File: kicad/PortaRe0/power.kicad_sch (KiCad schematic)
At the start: 18 parts, among them U1 BQ25895RTWR

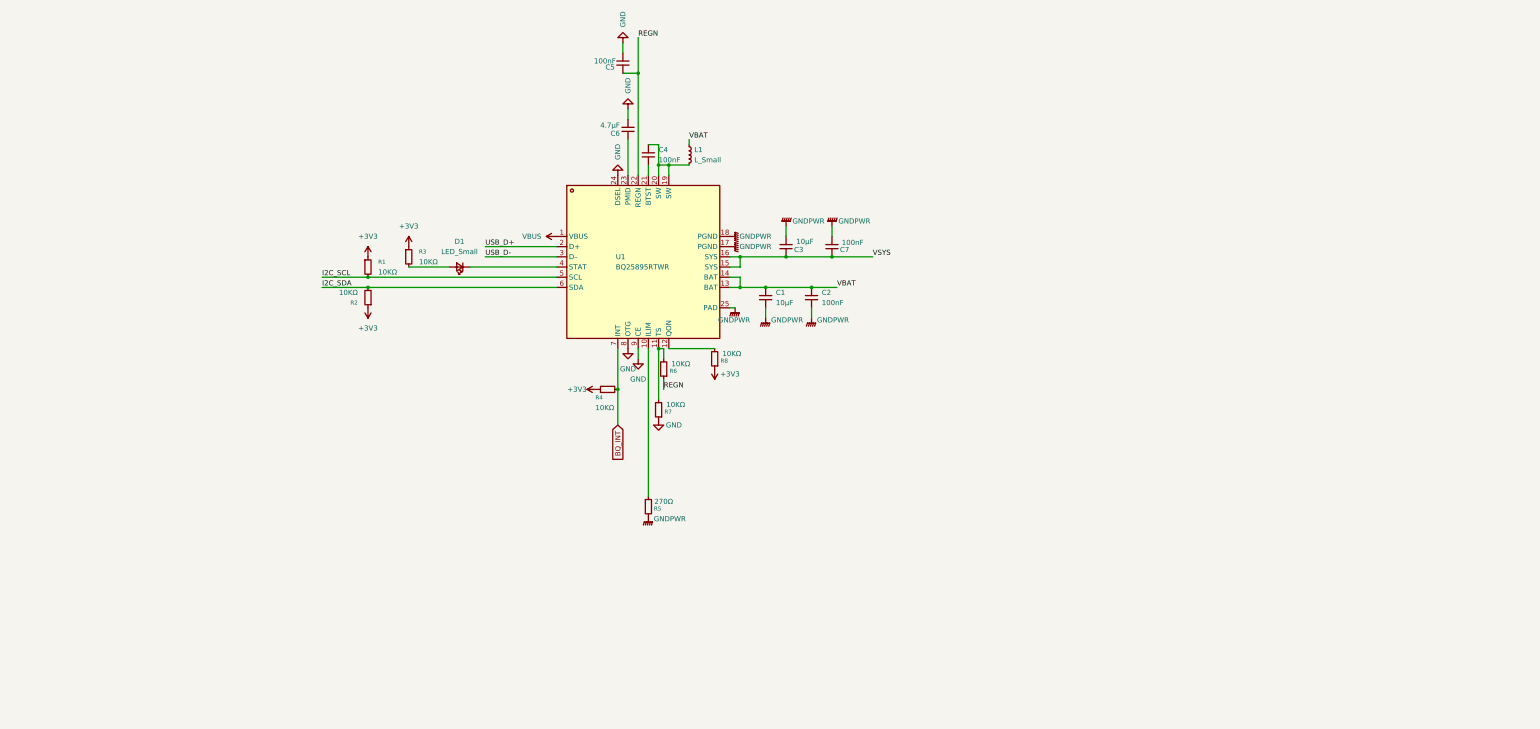
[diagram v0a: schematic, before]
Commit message: session06: TPS61023・AP2112K回路完成、VL812設計準備
- Claude.md: セッション開始時に最新ログを必ず読むよう更新
- PROGRESS.md: TPS61023・AP2112K完了に更新
- chat_logs/2026-02-20_session06.txt: セッション06ログ追加
- power.kicad_sch: TPS61023・AP2112K回路図追加

Co-Authored-By: Claude Sonnet 4.6 <noreply@anthropic.com>
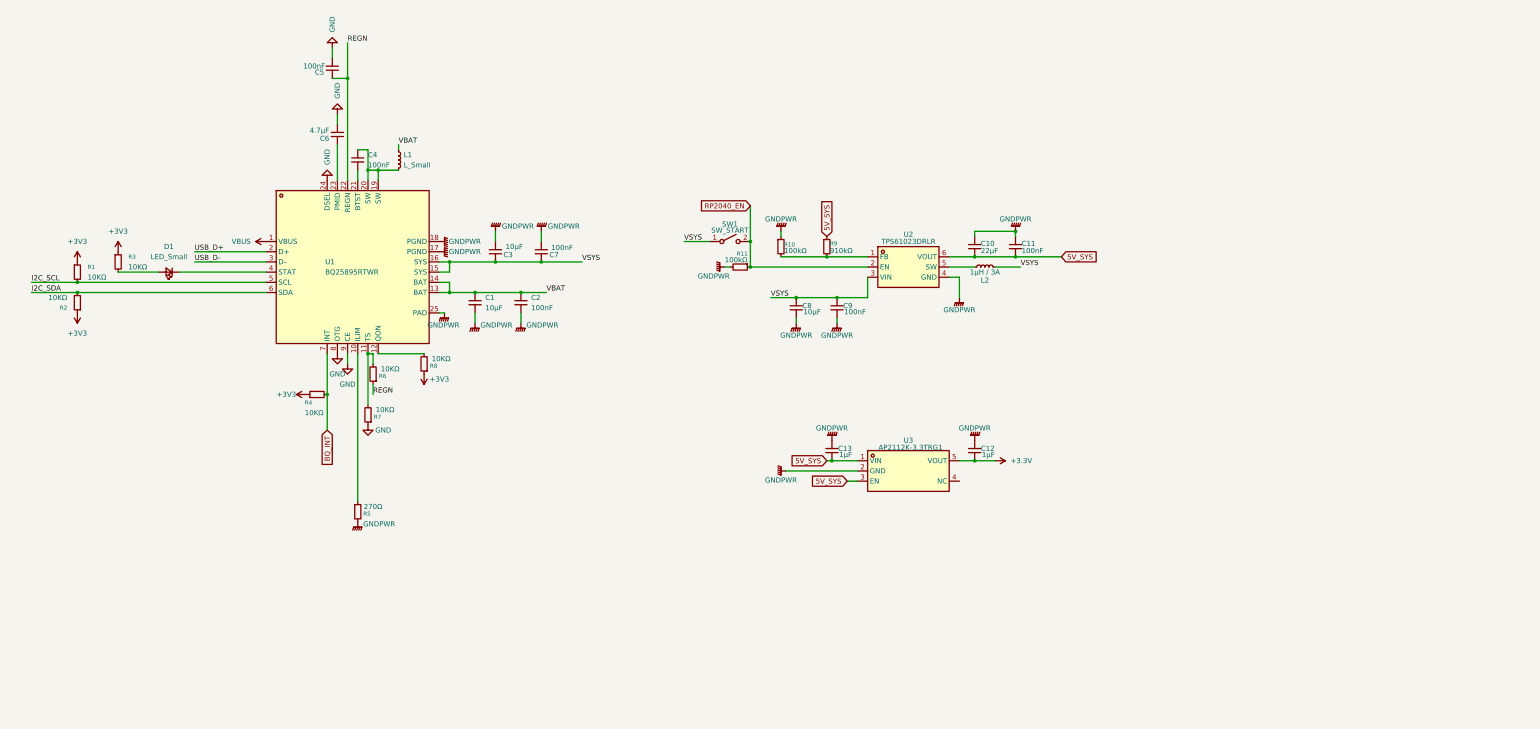
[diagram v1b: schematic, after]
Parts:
- added C10: 22µF, symbol Device:C_Small
- added C11, C9: 100nF, symbol Device:C_Small
- added C12, C13: 1µF, symbol Device:C_Small
- added C8: 10µF, symbol Device:C_Small
- added L2: 1µH / 3A, symbol Device:L_Small
- added R10, R11: 100kΩ, symbol Device:R_Small
- added R9: 910kΩ, symbol Device:R_Small
- added SW1: SW_START, symbol Switch:SW_SPST
- added U2: TPS61023DRLR, PortaRe0:SOT-563_L1.6-W1.2-P0.50-LS1.6-BR, symbol PortaRe0:TPS61023DRLR
- added U3: AP2112K-3.3TRG1, PortaRe0:SOT-25-5_L2.9-W1.6-P0.95-LS2.8-BL, symbol PortaRe0:AP2112K-3.3TRG1
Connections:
- net GNDPWR: now also C10.1, C11.1, C12.1, C13.1, C8.2, C9.2, R10.1, R11.2, U2.4 (GND), U3.2 (GND)
- net VSYS: now also C8.1, C9.1, L2.2, SW1.1 (A), U2.3 (VIN)
- new net: R10.2, R9.2, U2.1 (FB)
- new net: L2.1, U2.5 (SW)
- new net +3.3V: C12.2, U3.5 (VOUT)
- new net 5V_SYS: C10.2, C11.2, C13.2, R9.1, U2.6 (VOUT), U3.1 (VIN), U3.3 (EN)
- new net RP2040_EN: R11.1, SW1.2 (B), U2.2 (EN)
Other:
- moved on the sheet: C1, C2, C3, C4, C5, C6, C7, D1, L1, R1, R2, R3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

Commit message: session07: キーレイアウト確定・GPIO割り当て・power回路レビュー
- キーレイアウト確定（66キー / 9×8マトリクス）、keyboard-layout.json追加
- RP2040 GPIO割り当て確定（29本/30本）をPROJECT_PLANに追記
- power回路レビュー（5V_SYS→パワーシンボル化、SCL/SDA/USB_DP/USB_DM→GlobalLabel）
- .gitignoreに.claude/を追加

Co-Authored-By: Claude Sonnet 4.6 <noreply@anthropic.com>
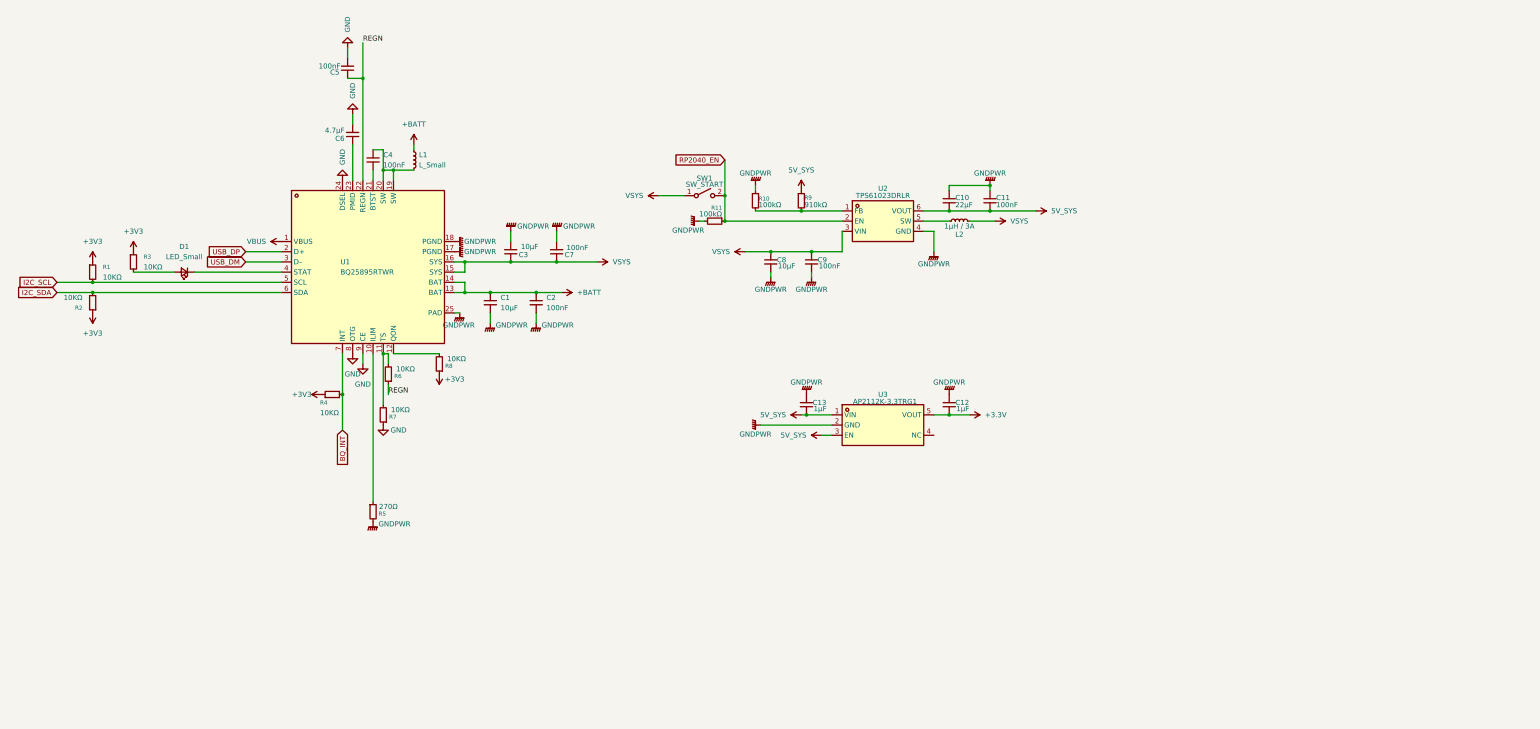
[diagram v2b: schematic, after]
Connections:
- net USB_D+ renamed USB_DP
- net USB_D- renamed USB_DM
- net VBAT renamed +BATT
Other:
- moved on the sheet: C1, C10, C11, C12, C13, C2, C3, C4, C5, C6, C7, C8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

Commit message: session07: VL812 usb_hubシート完成・power回路修正
- VL812 usb_hubシート完成
  - 電源ピン・デカップリングC配置
  - USB3.0 TX側ACカップリング・USB2.0直結
  - SPI Flash（W25Q32）接続・プルダウン
  - 水晶発振子（25MHz）追加
  - USBHOC1#/2# プルアップ追加（過電流誤検知防止）
- power回路: SCL/SDA/USB_DP/USB_DM GlobalLabel追加
- VL812データシート追加

Co-Authored-By: Claude Sonnet 4.6 <noreply@anthropic.com>
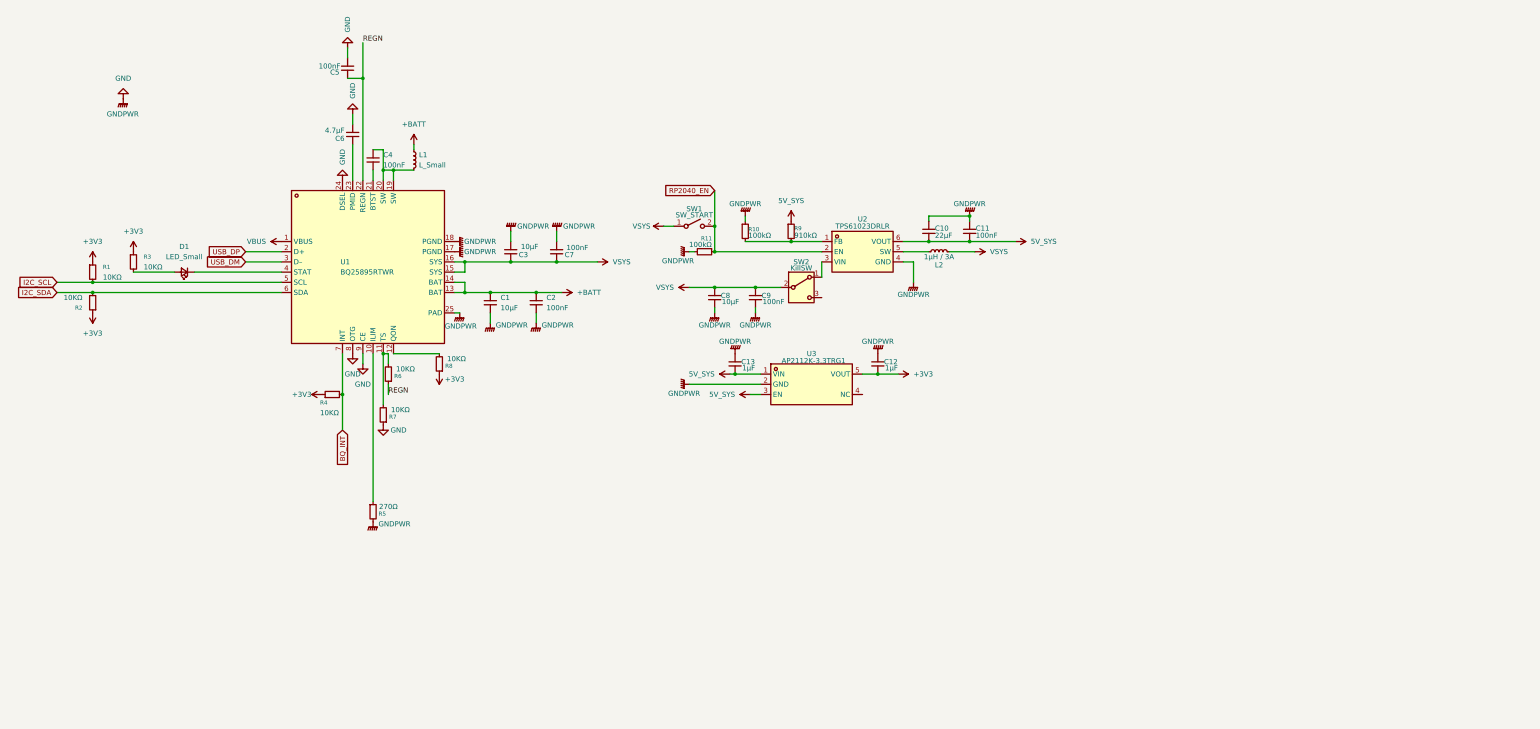
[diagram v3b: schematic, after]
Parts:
- added SW2: KillSW, symbol Switch:SW_SPDT
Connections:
- net +3.3V is gone; now on net +3V3: C12.2, U3.5 (VOUT)
- net GNDPWR is gone; now on net GND: C1.2, C10.1, C11.1, C12.1, C13.1, C2.2, C3.2, C7.2, C8.2, C9.2, R10.1, R11.2, R5.2, U1.17 (PGND), U1.18 (PGND), U1.25 (PAD), U2.4 (GND), U3.2 (GND)
- net VSYS: now also SW2.2 (B); no longer U2.3 (VIN)
- new net: SW2.1 (A), U2.3 (VIN)
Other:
- moved on the sheet: C10, C11, C12, C13, C8, C9, L2, R10, R11, R9, SW1, U2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

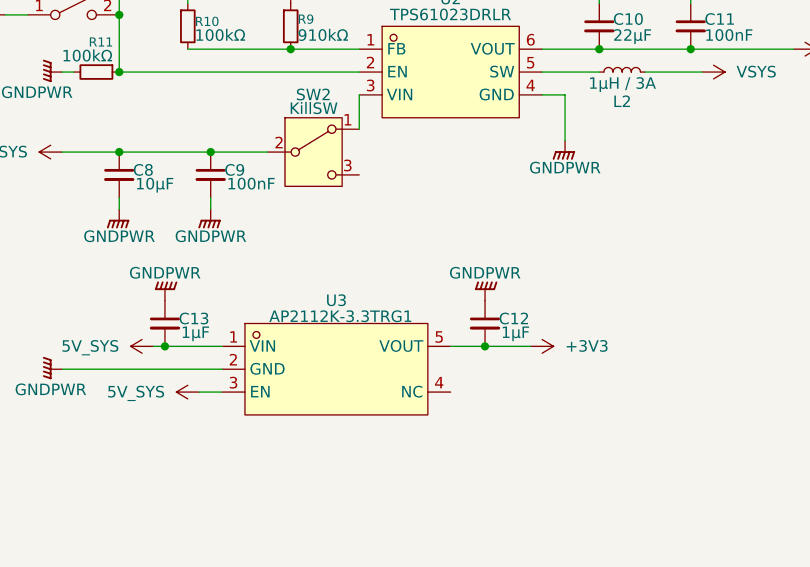
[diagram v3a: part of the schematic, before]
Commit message: session10: audio sheet完成、USB命名規則統一、TESTEN修正
- audio.kicad_sch: RP2040 #2追加、MAX98357A×2、PCM5102APWR、TPA6132A2RTER配線完了
- PCM5102APWR/TPA6132A2RTERシンボル・フットプリント追加
- I2S共有バス(BCLK/LRCLK/SDIN)でスピーカー・イヤホン共通接続
- GPIO割り当て: GP0-2=I2S, GP3=SD_MODE, GP4=XSMT, GP5=HP_EN, GP6=HP_DET
- USB命名規則統一: RP2040 #1→USB2_RP_DP/DM, RP2040 #2→USB2_RP_DP2/DM2
- VL812 USBHP4にUSB2_RP_DP2/DM2追加
- RP2040 #1/#2のTESTEN→GND修正
- BQ25895 D+/D-はUSB_DP/DM(充電用USB-C)で確定

Co-Authored-By: Claude Sonnet 4.6 <noreply@anthropic.com>
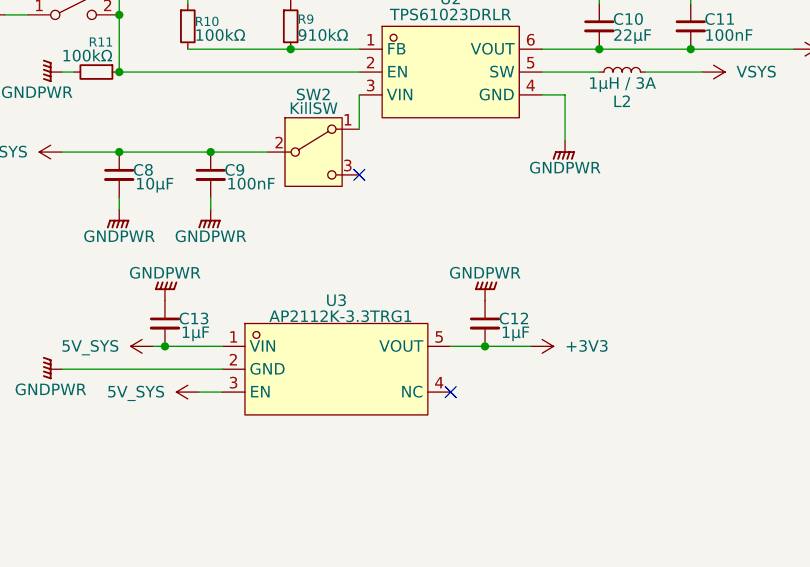
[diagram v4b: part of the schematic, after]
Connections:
- no-connect marks 0 -> 2
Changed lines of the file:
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@@
 		(color 0 0 0 0)
+	)
+	(no_connect
+		(at 213.36 85.09)
+	)
+	(no_connect
+		(at 223.52 109.22)
 	)
 	(wire

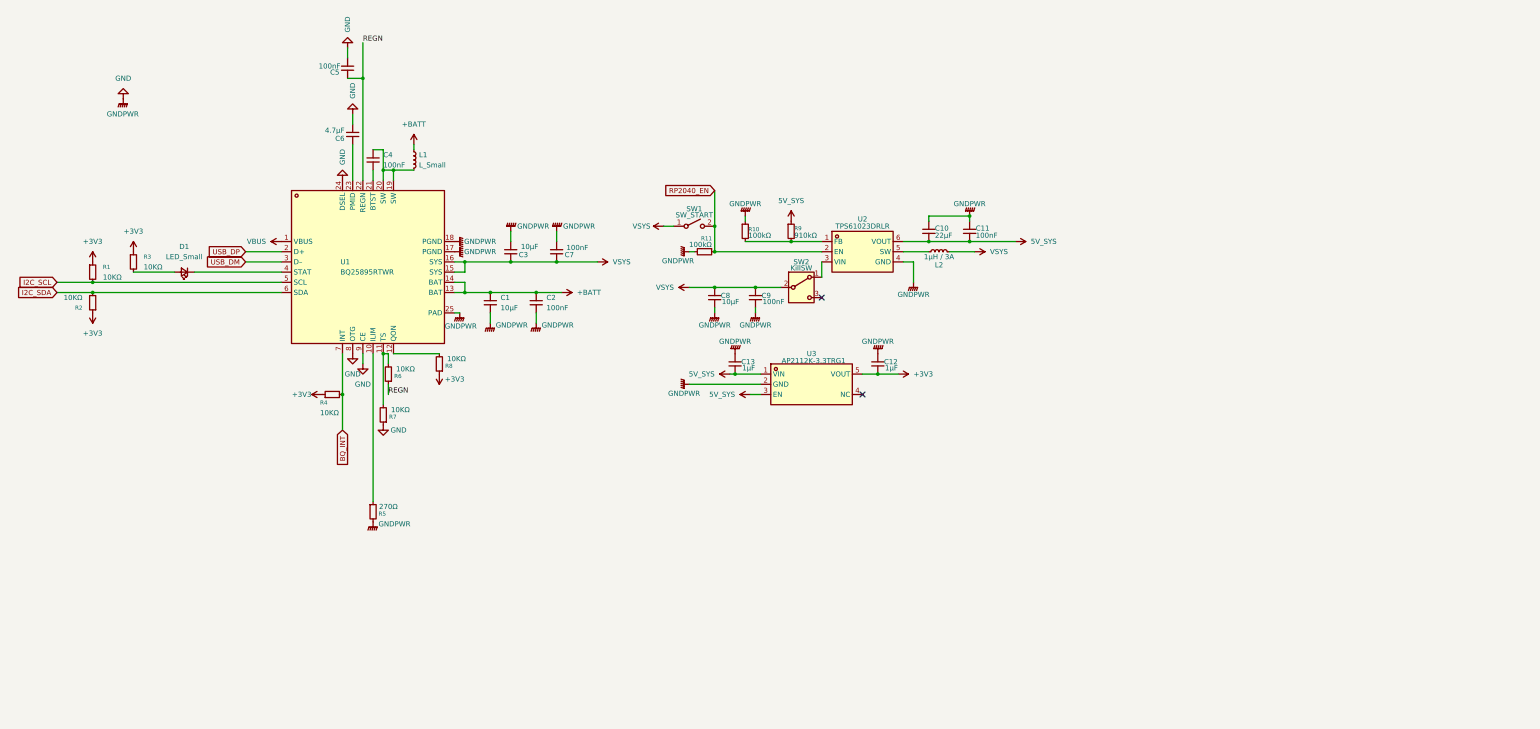
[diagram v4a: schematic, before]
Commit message: Docs: session15終了処理・PROGRESS/index更新・powerシート修正完了
- powerシートGemini評価検証・修正完了
  - L1接続変更: +BATT → VSYS (NVDC正しいトポロジー)
  - D1極性修正・R3 10kΩ→330Ω
  - SW1保護: BAT54(C466635)をGP20→ENノード間に挿入
  - ENノード10µFラッチキャップ追加
  - SW_DET回路追加: SW1→10kΩ分圧→GP25
  - C5 100nF→4.7µF / C6 4.7µF→10µF / SYSキャップ+10µF
- BAT54(C466635)シンボル/フットプリント追加
- GP25割り当て: 予備→SW_DET

Co-Authored-By: Claude Sonnet 4.6 <noreply@anthropic.com>
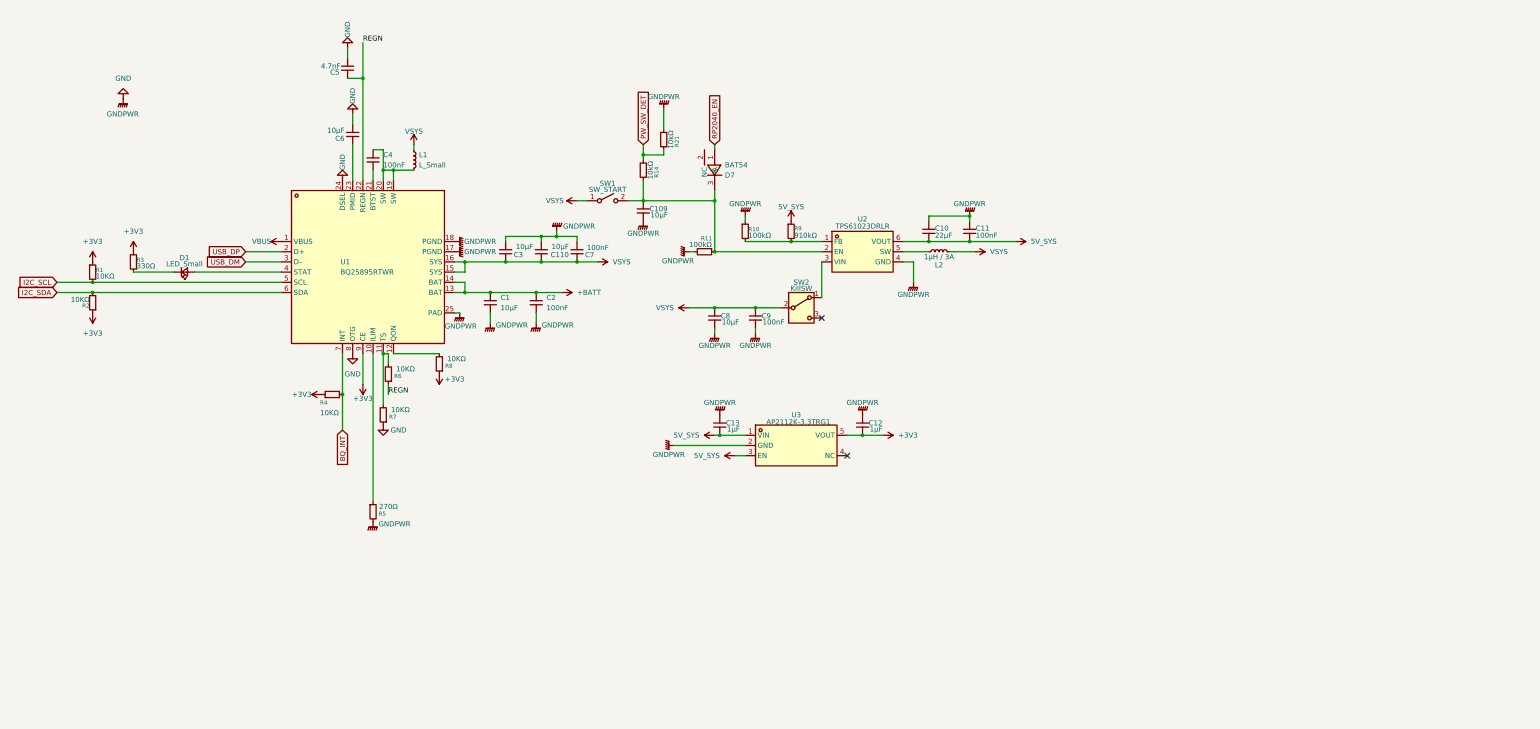
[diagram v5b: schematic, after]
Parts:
- added C109: 10µF, symbol Device:C_Small
- added C110: 10μF, symbol Device:C_Small
- added D7: BAT54, PortaRe0:SOT-23-3_L2.9-W1.4-P1.90-LS2.6-BR, symbol PortaRe0:BAT54_C466635
- added R14, R21: 10kΩ, symbol Device:R_Small
- C5: value 100nF -> 4.7nF
- C6: value 4.7µF -> 10µF
- R3: value 10KΩ -> 330Ω
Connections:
- net +3V3: now also U1.9 (CE)
- net +BATT: no longer L1.1
- net GND: now also C109.2, C110.2, R21.2; no longer U1.9 (CE)
- net RP2040_EN: now also D7.1 (A); no longer R11.1, SW1.2 (B), U2.2 (EN)
- net VSYS: now also L1.1, C110.1
- net at R3.2: now also D1.1 (K); no longer D1.2 (A)
- net at U1.4 (STAT): now also D1.2 (A); no longer D1.1 (K)
- new net: C109.1, D7.3 (K), R11.1, R14.1, SW1.2 (B), U2.2 (EN)
- new net PW_SW_DET: R14.2, R21.1
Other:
- moved on the sheet: C12, C13, C3, C7, C8, C9, D1, SW1, SW2, U3
